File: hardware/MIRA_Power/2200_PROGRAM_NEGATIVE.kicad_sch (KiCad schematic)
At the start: 25 parts, among them Q2201 AO3400A, Q2202 AO3400A, Q2203 AO3400A, Q2204 AO3401A, U2201 LTV-356T-A, U2202 LTV-356T-A, U2203 LTV-356T-A

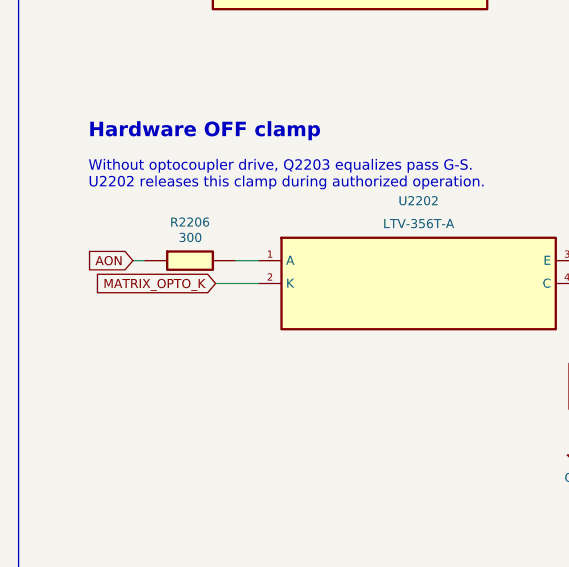
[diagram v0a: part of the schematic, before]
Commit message: Add high-load schematic candidate with CORE sense and revised N15 supply
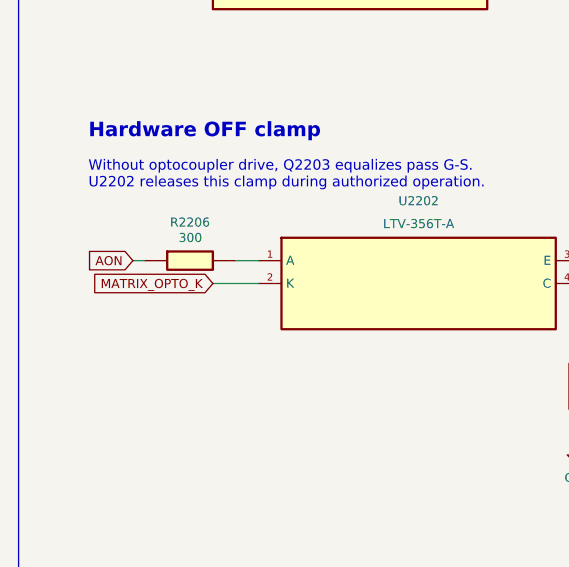
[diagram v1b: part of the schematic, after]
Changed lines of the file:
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@@
 	(wire
 		(pts
-			(xy 37.13 101.6) (xy 41.91 101.6)
+			(xy 36.83 101.6) (xy 41.91 101.6)
 		)
 		(stroke
@@
 	(global_label "MATRIX_OPTO_K"
 		(shape input)
-		(at 37.13 101.6 180)
-		(effects
-			(font
-				(size 1 1)
-			)
-			(justify right)
-		)
-		(property "Intersheetrefs" "${INTERSHEET_REFS}"
-			(at 37.13 101.6 0)
-			(hide yes)
-			(show_name no)
+		(at 36.83 101.6 180)
+		(effects
+			(font
+				(size 1 1)
+			)
+			(justify right)
+		)
+		(property "Intersheetrefs" "${INTERSHEET_REFS}"
+			(at 36.83 101.6 0)
+			(hide yes)
+			(show_name no)
